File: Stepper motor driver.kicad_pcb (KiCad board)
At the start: 2 copper layers, 63 x 74.4 mm, 24 parts, among them Q1 TIP120, Q2 TIP120, Q3 TIP120, Q4 TIP120, U1 74LS175, U2 74LS157

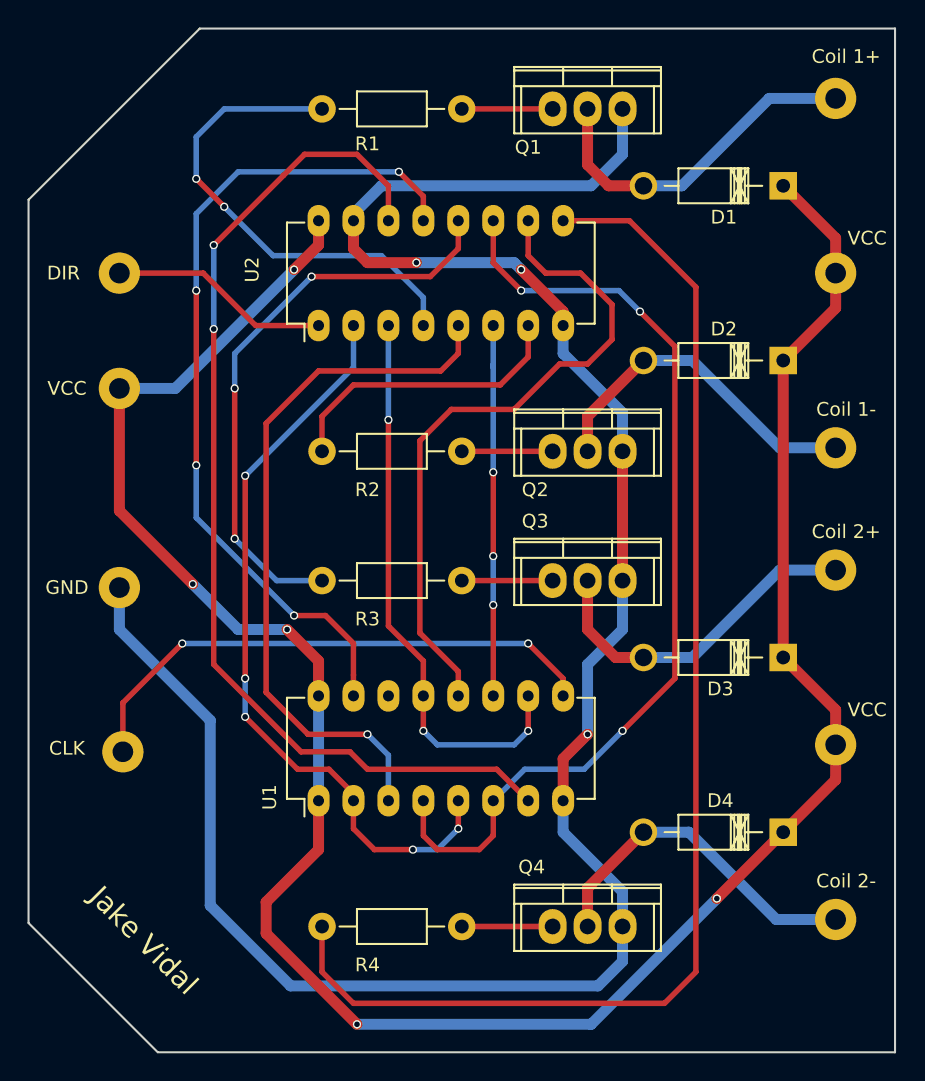
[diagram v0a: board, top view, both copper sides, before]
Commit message: touched up schematic and PCB, added ground pour, updated gerber and image files
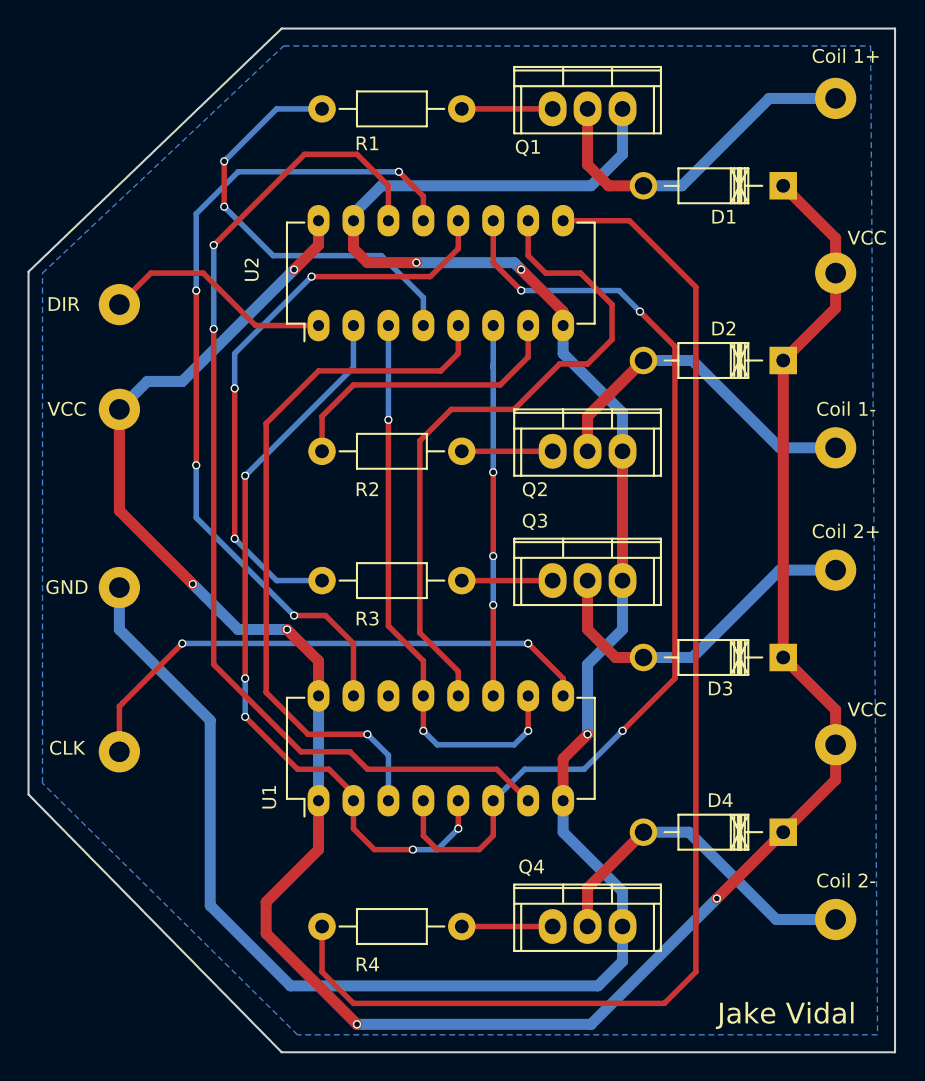
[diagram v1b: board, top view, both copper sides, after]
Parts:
- moved DIR 2.29 mm to (203.2, 40.4)
- moved VCC 1.52 mm to (203.2, 48.0)
- moved CLK 0.25 mm to (203.2, 72.9)
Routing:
- net Net-(R1-Pad2): track 35.2 -> 31.2 mm
- net /DIR: track 16.1 -> 17.0 mm
- net VCC: track 169.3 -> 168.4 mm
- added copper zone on B.Cu, net GND
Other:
- outline, holes or cut-outs redrawn

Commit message: added a second ground layer to distribute current
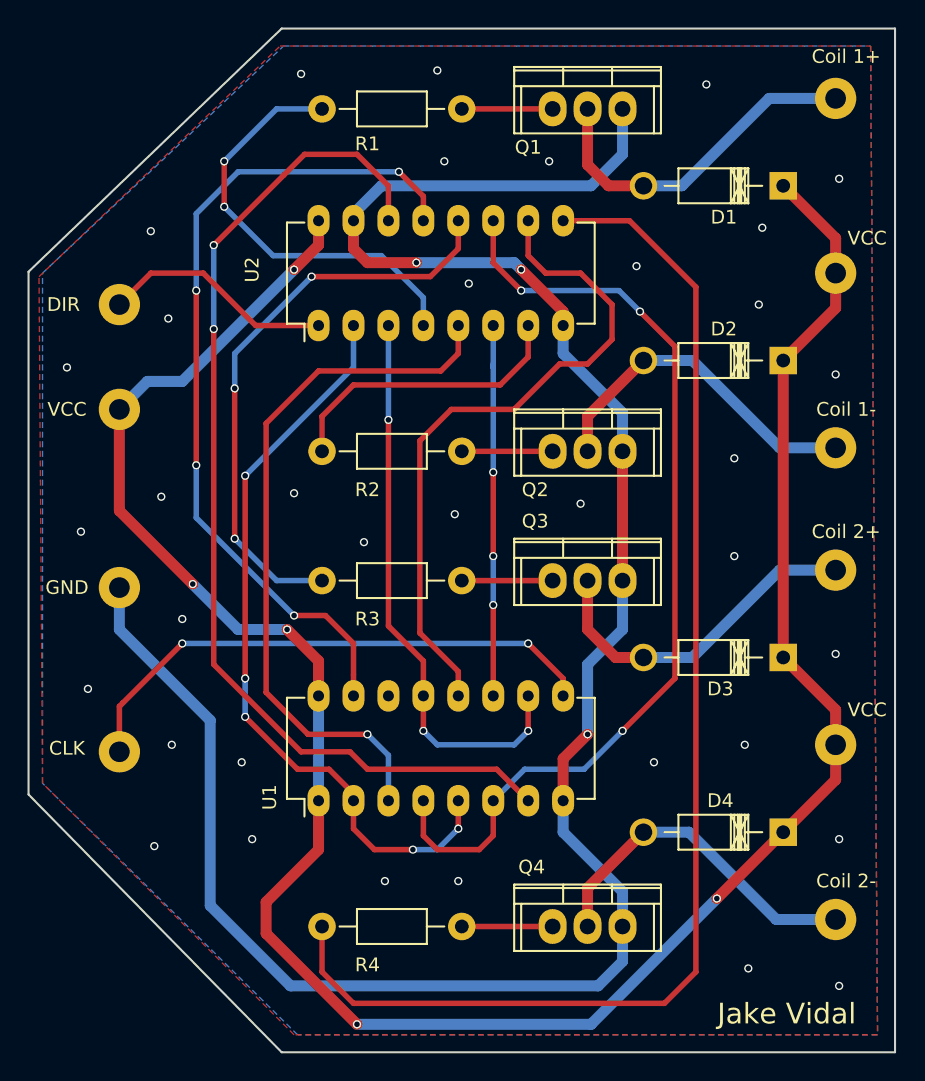
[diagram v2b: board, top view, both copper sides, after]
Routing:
- net GND: vias 3 -> 39
- added copper zone on F.Cu, net GND
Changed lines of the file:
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@@
     (thickness 1.6)
     (drawings 7)
-    (tracks 254)
+    (tracks 290)
     (zones 0)
     (modules 24)
@@
   (segment (start 237.236 85.598) (end 237.236 82.80654) (width 0.8) (layer F.Cu) (net 4))
   (segment (start 237.236 82.80654) (end 241.3 78.74254) (width 0.8) (layer F.Cu) (net 4))
+  (via (at 228.6 38.862) (size 0.6) (drill 0.4) (layers F.Cu B.Cu) (net 5))
+  (via (at 240.792 37.592) (size 0.6) (drill 0.4) (layers F.Cu B.Cu) (net 5))
+  (via (at 255.524 89.916) (size 0.6) (drill 0.4) (layers F.Cu B.Cu) (net 5))
+  (via (at 207.01 72.39) (size 0.6) (drill 0.4) (layers F.Cu B.Cu) (net 5))
+  (via (at 212.09 73.66) (size 0.6) (drill 0.4) (layers F.Cu B.Cu) (net 5))
+  (via (at 207.772 63.246) (size 0.6) (drill 0.4) (layers F.Cu B.Cu) (net 5))
+  (via (at 200.914 68.326) (size 0.6) (drill 0.4) (layers F.Cu B.Cu) (net 5))
+  (via (at 200.406 56.896) (size 0.6) (drill 0.4) (layers F.Cu B.Cu) (net 5))
+  (via (at 206.248 54.356) (size 0.6) (drill 0.4) (layers F.Cu B.Cu) (net 5))
+  (via (at 206.756 41.402) (size 0.6) (drill 0.4) (layers F.Cu B.Cu) (net 5))
+  (via (at 199.39 44.958) (size 0.6) (drill 0.4) (layers F.Cu B.Cu) (net 5))
+  (via (at 205.486 35.052) (size 0.6) (drill 0.4) (layers F.Cu B.Cu) (net 5))
+  (via (at 216.408 23.622) (size 0.6) (drill 0.4) (layers F.Cu B.Cu) (net 5))
+  (via (at 226.314 23.368) (size 0.6) (drill 0.4) (layers F.Cu B.Cu) (net 5))
+  (via (at 226.822 29.972) (size 0.6) (drill 0.4) (layers F.Cu B.Cu) (net 5))
+  (via (at 234.442 29.972) (size 0.6) (drill 0.4) (layers F.Cu B.Cu) (net 5))
+  (via (at 245.872 24.384) (size 0.6) (drill 0.4) (layers F.Cu B.Cu) (net 5))
+  (via (at 255.524 31.242) (size 0.6) (drill 0.4) (layers F.Cu B.Cu) (net 5))
+  (via (at 249.936 34.798) (size 0.6) (drill 0.4) (layers F.Cu B.Cu) (net 5))
+  (via (at 249.682 40.386) (size 0.6) (drill 0.4) (layers F.Cu B.Cu) (net 5))
+  (via (at 255.27 45.466) (size 0.6) (drill 0.4) (layers F.Cu B.Cu) (net 5))
+  (via (at 215.9 54.102) (size 0.6) (drill 0.4) (layers F.Cu B.Cu) (net 5))
+  (via (at 220.98 57.658) (size 0.6) (drill 0.4) (layers F.Cu B.Cu) (net 5))
+  (via (at 227.584 55.626) (size 0.6) (drill 0.4) (layers F.Cu B.Cu) (net 5))
+  (via (at 236.728 54.864) (size 0.6) (drill 0.4) (layers F.Cu B.Cu) (net 5))
+  (via (at 247.904 51.562) (size 0.6) (drill 0.4) (layers F.Cu B.Cu) (net 5))
+  (via (at 247.904 58.674) (size 0.6) (drill 0.4) (layers F.Cu B.Cu) (net 5))
+  (via (at 255.27 65.786) (size 0.6) (drill 0.4) (layers F.Cu B.Cu) (net 5))
+  (via (at 242.062 73.66) (size 0.6) (drill 0.4) (layers F.Cu B.Cu) (net 5))
+  (via (at 248.666 72.39) (size 0.6) (drill 0.4) (layers F.Cu B.Cu) (net 5))
+  (via (at 255.524 79.248) (size 0.6) (drill 0.4) (layers F.Cu B.Cu) (net 5))
+  (via (at 248.92 88.646) (size 0.6) (drill 0.4) (layers F.Cu B.Cu) (net 5))
+  (via (at 227.838 82.296) (size 0.6) (drill 0.4) (layers F.Cu B.Cu) (net 5))
+  (via (at 222.504 82.296) (size 0.6) (drill 0.4) (layers F.Cu B.Cu) (net 5))
+  (via (at 212.852 79.248) (size 0.6) (drill 0.4) (layers F.Cu B.Cu) (net 5))
+  (via (at 205.74 79.756) (size 0.6) (drill 0.4) (layers F.Cu B.Cu) (net 5))
   (segment (start 220.218 34.29) (end 220.218 33.782) (width 0.8) (layer B.Cu) (net 5))
   (segment (start 220.218 33.782) (end 222.25 31.75) (width 0.8) (layer B.Cu) (net 5))
@@
   (segment (start 213.106 41.91) (end 209.296 38.1) (width 0.4) (layer F.Cu) (net 24))
   (segment (start 217.678 41.91) (end 213.106 41.91) (width 0.4) (layer F.Cu) (net 24))
-  (segment (start 205.486 38.1) (end 203.2 40.386) (width 0.4) (layer F.Cu) (net 24) (status 800000))
+  (segment (start 205.486 38.1) (end 203.2 40.386) (width 0.4) (layer F.Cu) (net 24))
   (zone (net 5) (net_name GND) (layer B.Cu) (hatch edge 0.508)
     (connect_pads (clearance 0.508))
@@
         (xy 257.81 21.59) (xy 258.318 93.472)
       )
+    )
+  )
+  (zone (net 5) (net_name GND) (layer F.Cu) (hatch edge 0.508)
+    (connect_pads (clearance 0.508))
+    (min_thickness 0.254)
+    (fill yes (arc_segments 16) (thermal_gap 0.508) (thermal_bridge_width 0.508))
+    (polygon
+      (pts
+        (xy 258.318 93.472) (xy 215.9 93.472) (xy 197.612 75.184) (xy 197.358 38.354) (xy 214.884 21.59)
+        (xy 257.81 21.59) (xy 258.318 93.472)
+      )
